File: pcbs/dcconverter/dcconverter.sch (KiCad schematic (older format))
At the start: 42 parts, among them IC1 NCP7805TG, J1 190-9991, J3 146-8335, J4 766-6604, J5 766-6604, Q1 NGTB40N120FL2WG, Q10 TS13003CT, Q2 FQP47P06, Q3 2SK3747-1E, Q4 2SK3747-1E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

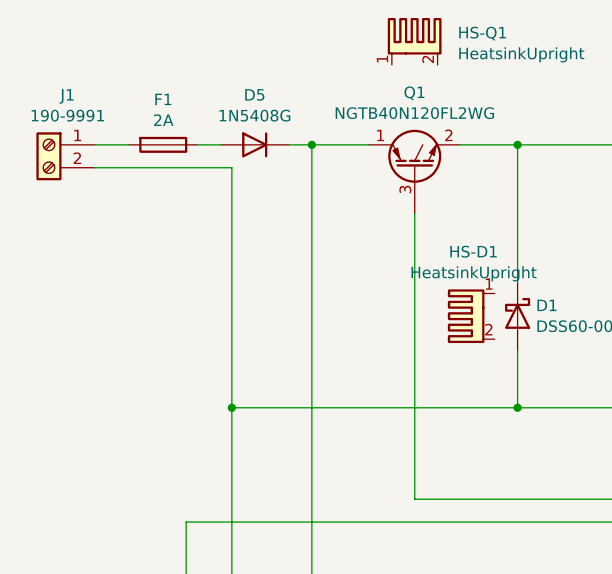
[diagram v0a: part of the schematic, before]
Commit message: Add measurement of input voltage
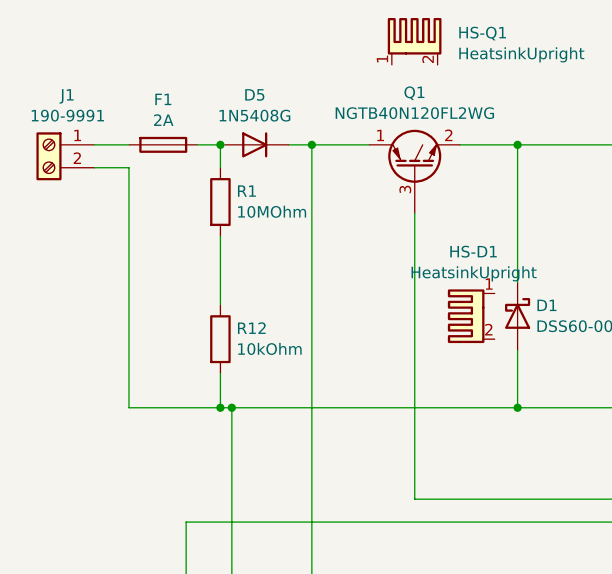
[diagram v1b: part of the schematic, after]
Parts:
- added R1: 10MOhm, Resistor_THT:R_Axial_DIN0207_L6.3mm_D2.5mm_P10.16mm_Horizontal, symbol Device:R
- added R12: 10kOhm, Resistor_THT:R_Axial_DIN0207_L6.3mm_D2.5mm_P10.16mm_Horizontal, symbol Device:R
- D5: footprint Diode_THT:D_5W_P12.70mm_Horizontal -> Custom:1N5408G
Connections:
- net at C1.2, C3.2, C5.2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: now also R12.2
- net at D5.2 (A), F1.1: now also R1.1
- new net: R1.2, R12.1
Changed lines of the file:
@@
 Wire Wire Line
 	2900 3100 2900 2850
-Wire Wire Line
-	1050 2050 1650 2050
 Connection ~ 2900 3100
 $Comp
@@
 F 0 "D5" H 1750 2167 50  0000 C CNN
 F 1 "1N5408G" H 1750 2076 50  0000 C CNN
-F 2 "Diode_THT:D_5W_P12.70mm_Horizontal" H 1750 1950 50  0001 C CNN
+F 2 "Custom:1N5408G" H 1750 1950 50  0001 C CNN
 F 3 "~" H 1750 1950 50  0001 C CNN
 	1    1750 1950
@@
 Connection ~ 2000 1950
 Wire Wire Line
-	1650 3100 1650 2050
+	1650 3100 2900 3100
+$Comp
+L Device:R R1
+U 1 1 5FBBC80C
+P 1600 2200
+F 0 "R1" H 1670 2246 50  0000 L CNN
+F 1 "10MOhm" H 1670 2155 50  0000 L CNN
+F 2 "Resistor_THT:R_Axial_DIN0207_L6.3mm_D2.5mm_P10.16mm_Horizontal" V 1530 2200 50  0001 C CNN
+F 3 "~" H 1600 2200 50  0001 C CNN
+	1    1600 2200
+	1    0    0    -1
+$EndComp
+$Comp
+L Device:R R12
+U 1 1 5FBBD1DD
+P 1600 2800
+F 0 "R12" H 1670 2846 50  0000 L CNN
+F 1 "10kOhm" H 1670 2755 50  0000 L CNN
+F 2 "Resistor_THT:R_Axial_DIN0207_L6.3mm_D2.5mm_P10.16mm_Horizontal" V 1530 2800 50  0001 C CNN
+F 3 "~" H 1600 2800 50  0001 C CNN
+	1    1600 2800
+	1    0    0    -1
+$EndComp
+Wire Wire Line
+	1600 1950 1600 2050
+Connection ~ 1600 1950
+Wire Wire Line
+	1600 2350 1600 2650
+Wire Wire Line
+	1600 2950 1600 3100
+Wire Wire Line
+	1600 3100 1650 3100
 Connection ~ 1650 3100
 Wire Wire Line
-	1650 3100 2900 3100
+	1600 3100 1200 3100
+Wire Wire Line
+	1200 3100 1200 2050
+Wire Wire Line
+	1200 2050 1050 2050
+Connection ~ 1600 3100
 $EndSCHEMATC

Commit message: Fix minor stuff
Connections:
- net at D5.1 (K), Q1.1 (C), Q3.3 (D)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: now also R1.1
- net at D5.2 (A), F1.1: no longer R1.1
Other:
- moved on the sheet: D5, F1, R1, R12
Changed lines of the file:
@@
 L Device:Fuse F1
 U 1 1 5F93C935
-P 1350 1950
-F 0 "F1" V 1153 1950 50  0000 C CNN
-F 1 "2A" V 1244 1950 50  0000 C CNN
-F 2 "Fuse:Fuseholder_Cylinder-5x20mm_Schurter_0031_8201_Horizontal_Open" V 1280 1950 50  0001 C CNN
-F 3 "~" H 1350 1950 50  0001 C CNN
-	1    1350 1950
-	0    1    1    0
-$EndComp
-Wire Wire Line
-	1050 1950 1200 1950
+P 1250 1950
+F 0 "F1" V 1053 1950 50  0000 C CNN
+F 1 "2A" V 1144 1950 50  0000 C CNN
+F 2 "Fuse:Fuseholder_Cylinder-5x20mm_Schurter_0031_8201_Horizontal_Open" V 1180 1950 50  0001 C CNN
+F 3 "~" H 1250 1950 50  0001 C CNN
+	1    1250 1950
+	0    1    1    0
+$EndComp
 $Comp
 L Device:D_Schottky D1
@@
 L Device:D D5
 U 1 1 5FBA5BAB
-P 1750 1950
-F 0 "D5" H 1750 2167 50  0000 C CNN
-F 1 "1N5408G" H 1750 2076 50  0000 C CNN
-F 2 "Custom:1N5408G" H 1750 1950 50  0001 C CNN
-F 3 "~" H 1750 1950 50  0001 C CNN
-	1    1750 1950
+P 1650 1950
+F 0 "D5" H 1650 2167 50  0000 C CNN
+F 1 "1N5408G" H 1650 2076 50  0000 C CNN
+F 2 "Custom:1N5408G" H 1650 1950 50  0001 C CNN
+F 3 "~" H 1650 1950 50  0001 C CNN
+	1    1650 1950
 	-1   0    0    -1
 $EndComp
-Wire Wire Line
-	1500 1950 1600 1950
-Wire Wire Line
-	1900 1950 2000 1950
 Connection ~ 2000 1950
 Wire Wire Line
-	1650 3100 2900 3100
+	1650 3100 1850 3100
 $Comp
 L Device:R R1
 U 1 1 5FBBC80C
-P 1600 2200
-F 0 "R1" H 1670 2246 50  0000 L CNN
-F 1 "10MOhm" H 1670 2155 50  0000 L CNN
-F 2 "Resistor_THT:R_Axial_DIN0207_L6.3mm_D2.5mm_P10.16mm_Horizontal" V 1530 2200 50  0001 C CNN
-F 3 "~" H 1600 2200 50  0001 C CNN
-	1    1600 2200
+P 1850 2200
+F 0 "R1" H 1920 2246 50  0000 L CNN
+F 1 "10MOhm" H 1920 2155 50  0000 L CNN
+F 2 "Resistor_THT:R_Axial_DIN0207_L6.3mm_D2.5mm_P10.16mm_Horizontal" V 1780 2200 50  0001 C CNN
+F 3 "~" H 1850 2200 50  0001 C CNN
+	1    1850 2200
 	1    0    0    -1
 $EndComp
@@
 L Device:R R12
 U 1 1 5FBBD1DD
-P 1600 2800
-F 0 "R12" H 1670 2846 50  0000 L CNN
-F 1 "10kOhm" H 1670 2755 50  0000 L CNN
-F 2 "Resistor_THT:R_Axial_DIN0207_L6.3mm_D2.5mm_P10.16mm_Horizontal" V 1530 2800 50  0001 C CNN
-F 3 "~" H 1600 2800 50  0001 C CNN
-	1    1600 2800
-	1    0    0    -1
-$EndComp
-Wire Wire Line
-	1600 1950 1600 2050
-Connection ~ 1600 1950
-Wire Wire Line
-	1600 2350 1600 2650
-Wire Wire Line
-	1600 2950 1600 3100
-Wire Wire Line
-	1600 3100 1650 3100
+P 1850 2800
+F 0 "R12" H 1920 2846 50  0000 L CNN
+F 1 "10kOhm" H 1920 2755 50  0000 L CNN
+F 2 "Resistor_THT:R_Axial_DIN0207_L6.3mm_D2.5mm_P10.16mm_Horizontal" V 1780 2800 50  0001 C CNN
+F 3 "~" H 1850 2800 50  0001 C CNN
+	1    1850 2800
+	1    0    0    -1
+$EndComp
+Wire Wire Line
+	1850 2350 1850 2650
 Connection ~ 1650 3100
 Wire Wire Line
-	1600 3100 1200 3100
-Wire Wire Line
 	1200 3100 1200 2050
 Wire Wire Line
 	1200 2050 1050 2050
-Connection ~ 1600 3100
+Wire Wire Line
+	1200 3100 1650 3100
+Wire Wire Line
+	1050 1950 1100 1950
+Wire Wire Line
+	1400 1950 1500 1950
+Wire Wire Line
+	1800 1950 1850 1950
+Wire Wire Line
+	1850 2050 1850 1950
+Connection ~ 1850 1950
+Wire Wire Line
+	1850 1950 2000 1950
+Wire Wire Line
+	1850 2950 1850 3100
+Connection ~ 1850 3100
+Wire Wire Line
+	1850 3100 2900 3100
 $EndSCHEMATC

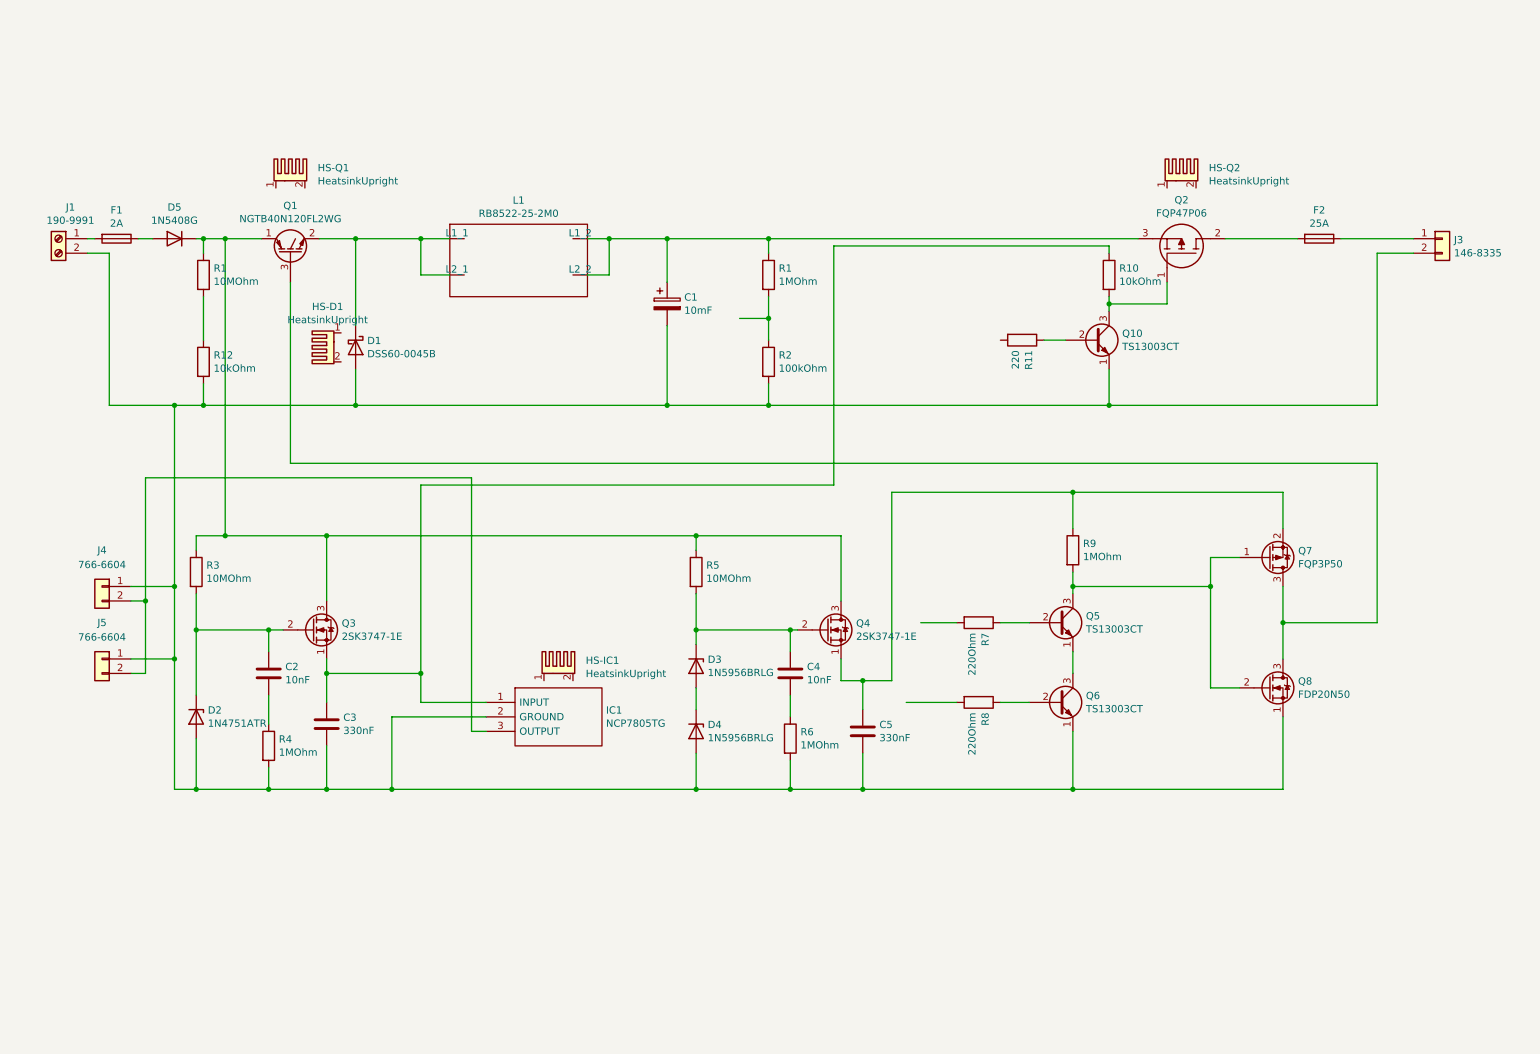
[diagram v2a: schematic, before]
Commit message: Add controller to PCB schematic
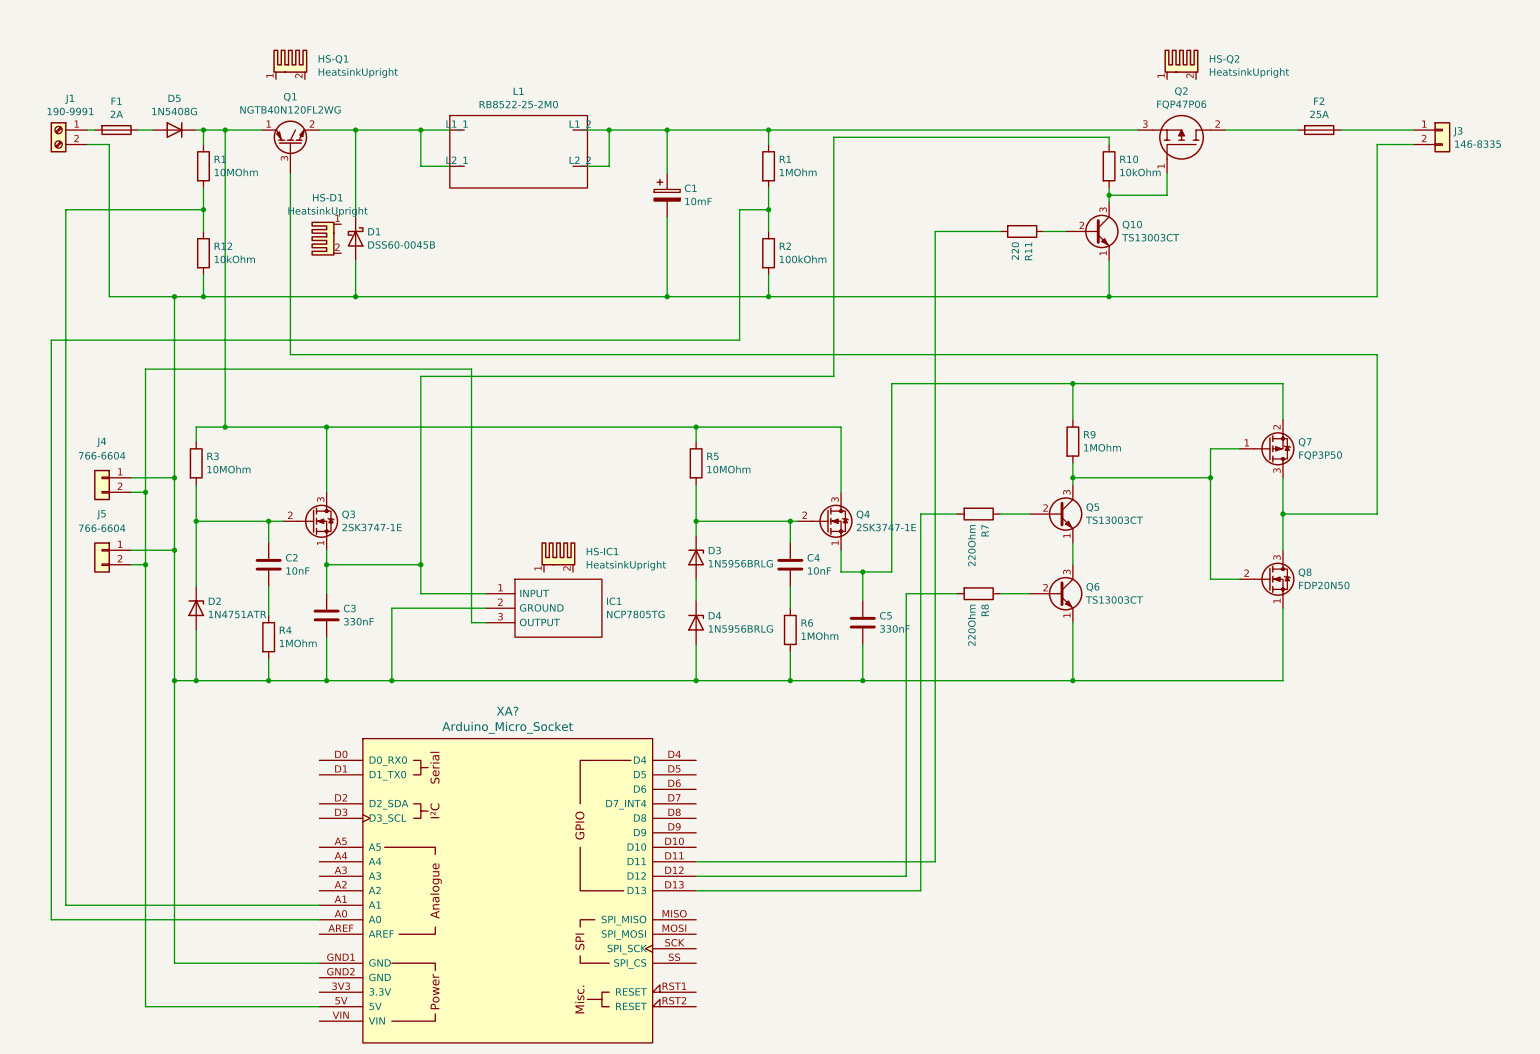
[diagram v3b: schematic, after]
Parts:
- added XA?: Arduino_Micro_Socket, Custom:Arduino_Micro_Socket, symbol Custom:Arduino_Micro_Socket
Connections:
- net at C1.2, C3.2, C5.2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: now also XA?.GND1 (GND)
- net at R1.2, R2.1: now also XA?.A0
- net at IC1.3 (OUTPUT), J4.2 (Pin_2), J5.2 (Pin_2): now also XA?.5V
- net at R7.2: now also XA?.D13
- net at R8.2: now also XA?.D12
- net at R11.2: now also XA?.D11
- net at R1.2, R12.1: now also XA?.A1
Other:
- moved on the sheet: C1, C2, C3, C4, C5, D1, D2, D3, D4, D5, F1, F2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

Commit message: Add banana sockets to DC converter schematic
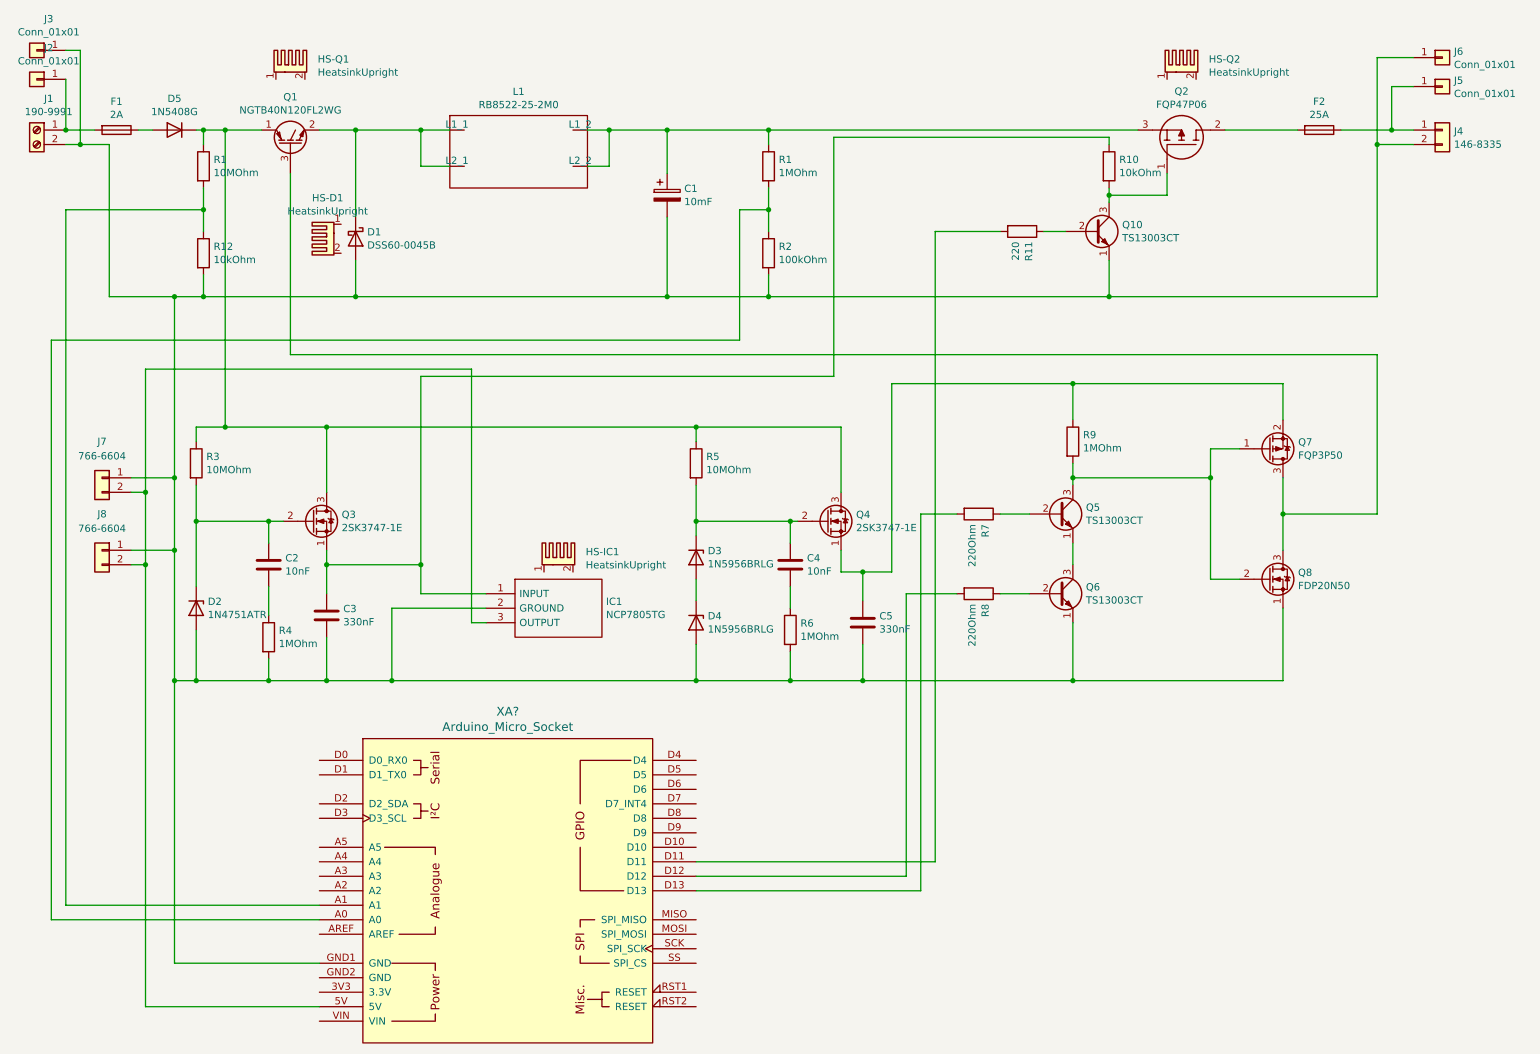
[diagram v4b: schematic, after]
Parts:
- added J2, J3, J5, J6: Conn_01x01, Custom:SLB4-I90, symbol Connector_Generic:Conn_01x01
- renumbered J3 to J4, J4 to J7, J5 to J8
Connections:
- net at F1.2, J1.1 (Pin_1): now also J2.1 (Pin_1)
- net at C1.2, C3.2, C5.2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: now also J3.1 (Pin_1), J6.1 (Pin_1)
- net at F2.1, J4.1 (Pin_1): now also J5.1 (Pin_1)
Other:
- moved on the sheet: J1
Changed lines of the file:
@@
 L Connector:Screw_Terminal_01x02 J1
 U 1 1 5F938BEF
-P 850 1200
-F 0 "J1" H 768 1417 50  0000 C CNN
-F 1 "190-9991" H 768 1326 50  0000 C CNN
-F 2 "Custom:TerminalBlock_2pin_10mm" H 850 1200 50  0001 C CNN
-F 3 "~" H 850 1200 50  0001 C CNN
-	1    850  1200
+P 700 1200
+F 0 "J1" H 618 1417 50  0000 C CNN
+F 1 "190-9991" H 618 1326 50  0000 C CNN
+F 2 "Custom:TerminalBlock_2pin_10mm" H 700 1200 50  0001 C CNN
+F 3 "~" H 700 1200 50  0001 C CNN
+	1    700  1200
 	-1   0    0    -1
 $EndComp
@@
 $EndComp
 $Comp
-L Connector_Generic:Conn_01x02 J3
+L Connector_Generic:Conn_01x02 J4
 U 1 1 5F94D2E0
 P 10400 1200
-F 0 "J3" H 10480 1192 50  0000 L CNN
+F 0 "J4" H 10480 1192 50  0000 L CNN
 F 1 "146-8335" H 10480 1101 50  0000 L CNN
 F 2 "Custom:connector_2pin_P10.6mm" H 10400 1200 50  0001 C CNN
@@
 $EndComp
 Wire Wire Line
-	10200 1200 9700 1200
+	10200 1200 10050 1200
 Wire Wire Line
 	9400 1200 8900 1200
@@
 	3700 2850 3700 4600
 $Comp
-L Connector_Generic:Conn_01x02 J4
+L Connector_Generic:Conn_01x02 J7
 U 1 1 5FA3A804
 P 1150 3600
-F 0 "J4" H 1150 3850 50  0000 C CNN
+F 0 "J7" H 1150 3850 50  0000 C CNN
 F 1 "766-6604" H 1150 3750 50  0000 C CNN
 F 2 "Custom:CES-102-XX-Y-S" H 1150 3600 50  0001 C CNN
@@
 $EndComp
 $Comp
-L Connector_Generic:Conn_01x02 J5
+L Connector_Generic:Conn_01x02 J8
 U 1 1 5FA5AA03
 P 1150 4100
-F 0 "J5" H 1150 4350 50  0000 C CNN
+F 0 "J8" H 1150 4350 50  0000 C CNN
 F 1 "766-6604" H 1150 4250 50  0000 C CNN
 F 2 "Custom:CES-102-XX-Y-S" H 1150 4100 50  0001 C CNN
@@
 	1200 2350 1200 1300
 Wire Wire Line
-	1200 1300 1050 1300
-Wire Wire Line
 	1200 2350 1650 2350
-Wire Wire Line
-	1050 1200 1100 1200
 Wire Wire Line
 	1400 1200 1500 1200
@@
 Wire Wire Line
 	6900 1900 7350 1900
+$Comp
+L Connector_Generic:Conn_01x01 J3
+U 1 1 5FC4664A
+P 700 650
+F 0 "J3" H 618 867 50  0000 C CNN
+F 1 "Conn_01x01" H 618 776 50  0000 C CNN
+F 2 "Custom:SLB4-I90" H 700 650 50  0001 C CNN
+F 3 "~" H 700 650 50  0001 C CNN
+	1    700  650
+	-1   0    0    -1
+$EndComp
+$Comp
+L Connector_Generic:Conn_01x01 J2
+U 1 1 5FC46DC5
+P 700 850
+F 0 "J2" H 618 1067 50  0000 C CNN
+F 1 "Conn_01x01" H 618 976 50  0000 C CNN
+F 2 "Custom:SLB4-I90" H 700 850 50  0001 C CNN
+F 3 "~" H 700 850 50  0001 C CNN
+	1    700  850
+	-1   0    0    -1
+$EndComp
+Wire Wire Line
+	900  850  900  1200
+Connection ~ 900  1200
+Wire Wire Line
+	900  1200 1100 1200
+Wire Wire Line
+	900  1300 1000 1300
+Wire Wire Line
+	900  650  1000 650
+Wire Wire Line
+	1000 650  1000 1300
+Connection ~ 1000 1300
+Wire Wire Line
+	1000 1300 1200 1300
+$Comp
+L Connector_Generic:Conn_01x01 J5
+U 1 1 5FC84274
+P 10400 900
+F 0 "J5" H 10480 942 50  0000 L CNN
+F 1 "Conn_01x01" H 10480 851 50  0000 L CNN
+F 2 "Custom:SLB4-I90" H 10400 900 50  0001 C CNN
+F 3 "~" H 10400 900 50  0001 C CNN
+	1    10400 900
+	1    0    0    -1
+$EndComp
+$Comp
+L Connector_Generic:Conn_01x01 J6
+U 1 1 5FC8CBC2
+P 10400 700
+F 0 "J6" H 10480 742 50  0000 L CNN
+F 1 "Conn_01x01" H 10480 651 50  0000 L CNN
+F 2 "Custom:SLB4-I90" H 10400 700 50  0001 C CNN
+F 3 "~" H 10400 700 50  0001 C CNN
+	1    10400 700
+	1    0    0    -1
+$EndComp
+Wire Wire Line
+	10200 700  9950 700
+Wire Wire Line
+	9950 700  9950 1300
+Connection ~ 9950 1300
+Wire Wire Line
+	10200 900  10050 900
+Wire Wire Line
+	10050 900  10050 1200
+Connection ~ 10050 1200
+Wire Wire Line
+	10050 1200 9700 1200
 $EndSCHEMATC
